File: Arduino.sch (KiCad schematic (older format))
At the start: 0 parts

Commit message: arduino module / hooking things up
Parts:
- added R? (x13): R, ~, symbol R
- added U?: ARDUINOPINS, symbol ARDUINOPINS
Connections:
- net MISO: now also R?.2
- net MOSI: now also R?.2
- net SCLK: now also R?.2
- net TACH_MEAS: now also R?.1
- new net: R?.1, U?.11 (Digital0)
- new net: R?.1, U?.12 (Digital1)
- new net: R?.1, U?.13 (Digital2)
- new net: R?.1, U?.19 (Digital8)
- new net: R?.1, U?.20 (PWM0)
- new net: R?.1, U?.21 (CS_N)
- new net: R?.1, U?.22 (MOSI)
- new net: R?.1, U?.23 (MISO)
- new net: R?.1, U?.24 (SCK)
- new net: R?.2, U?.5 (Analog0)
- new net: R?.2, U?.6 (Analog1)
- new net: R?.2, U?.7 (Analog2)
- new net: R?.2, U?.8 (Analog3)
- new net ADC_CS_N: R?.2
- new net CURR_MEAS: R?.1
- new net DAC_CS_N: R?.2
- new net FAN_EN_N: R?.2
- new net LED_EN_PWM: R?.2
- new net RELAY+: R?.2
- new net V+_ADJ_MON: R?.1
- new net V-_ADJ_MON: R?.1

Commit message: currentfan revisited
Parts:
- added R?: R, ~, symbol R
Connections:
- net at U?.11 (Digital0): now also R?.1; no longer R?.1
- net at U?.13 (Digital2): no longer R?.1
- net at U?.18 (Digital7): now also R?.1
- net at U?.21 (CS_N): now also R?.1; no longer R?.1
- net at U?.4 (9V): now also R?.2
- net FAN_MODE: now reaches R?.2
- net FAN_EN_N renamed FAN_PWM_N
- new net +12P: R?.1
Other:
- moved on the sheet: R?
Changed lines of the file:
@@
 Sheet 9 9
 Title ""
-Date "7 feb 2014"
+Date "10 feb 2014"
 Rev ""
 Comp ""
@@
 Text HLabel 6300 2950 2    60   Output ~ 0
 SCLK
-Text HLabel 6300 3400 2    60   Output ~ 0
+Text HLabel 6300 3850 2    60   Output ~ 0
 DAC_CS_N
 Text HLabel 6300 3550 2    60   Output ~ 0
 LED_EN_PWM
-Text HLabel 6300 4900 2    60   Output ~ 0
-FAN_EN_N
+Text HLabel 6300 3400 2    60   Output ~ 0
+FAN_PWM_N
 Text HLabel 2550 4600 0    60   Input ~ 0
 TACH_MEAS
@@
 L R R?
 U 1 1 52F5E804
-P 5900 4900
-F 0 "R?" V 5980 4900 40  0000 C CNN
-F 1 "R" V 5907 4901 40  0000 C CNN
-F 2 "~" V 5830 4900 30  0000 C CNN
-F 3 "~" H 5900 4900 30  0000 C CNN
-	1    5900 4900
-	0    -1   -1   0
-$EndComp
-Wire Wire Line
-	5450 4900 5650 4900
-Wire Wire Line
-	6150 4900 6300 4900
+P 5900 3400
+F 0 "R?" V 5980 3400 40  0000 C CNN
+F 1 "R" V 5907 3401 40  0000 C CNN
+F 2 "~" V 5830 3400 30  0000 C CNN
+F 3 "~" H 5900 3400 30  0000 C CNN
+	1    5900 3400
+	0    -1   -1   0
+$EndComp
+Wire Wire Line
+	5450 3400 5650 3400
+Wire Wire Line
+	6150 3400 6300 3400
 $Comp
 L R R?
@@
 L R R?
 U 1 1 52F5E82A
-P 5900 4600
-F 0 "R?" V 5980 4600 40  0000 C CNN
-F 1 "R" V 5907 4601 40  0000 C CNN
-F 2 "~" V 5830 4600 30  0000 C CNN
-F 3 "~" H 5900 4600 30  0000 C CNN
-	1    5900 4600
-	0    -1   -1   0
-$EndComp
-Wire Wire Line
-	5450 4600 5650 4600
-Wire Wire Line
-	6150 4600 6300 4600
+P 5900 4900
+F 0 "R?" V 5980 4900 40  0000 C CNN
+F 1 "R" V 5907 4901 40  0000 C CNN
+F 2 "~" V 5830 4900 30  0000 C CNN
+F 3 "~" H 5900 4900 30  0000 C CNN
+	1    5900 4900
+	0    -1   -1   0
+$EndComp
+Wire Wire Line
+	5450 4900 5650 4900
+Wire Wire Line
+	6150 4900 6300 4900
 Wire Wire Line
 	6300 4750 6150 4750
@@
 L R R?
 U 1 1 52F61E12
-P 5900 3400
-F 0 "R?" V 5980 3400 40  0000 C CNN
-F 1 "R" V 5907 3401 40  0000 C CNN
-F 2 "~" V 5830 3400 30  0000 C CNN
-F 3 "~" H 5900 3400 30  0000 C CNN
-	1    5900 3400
-	0    -1   -1   0
-$EndComp
-Wire Wire Line
-	6300 3400 6150 3400
-Wire Wire Line
-	5650 3400 5450 3400
+P 5900 3850
+F 0 "R?" V 5980 3850 40  0000 C CNN
+F 1 "R" V 5907 3851 40  0000 C CNN
+F 2 "~" V 5830 3850 30  0000 C CNN
+F 3 "~" H 5900 3850 30  0000 C CNN
+	1    5900 3850
+	0    -1   -1   0
+$EndComp
+Wire Wire Line
+	6300 3850 6150 3850
+Wire Wire Line
+	5650 3850 5450 3850
 $Comp
 L R R?
@@
 Wire Wire Line
 	5650 3700 5450 3700
+Text HLabel 6300 4900 2    60   Output ~ 0
+FAN_MODE
+$Comp
+L R R?
+U 1 1 52F919D6
+P 3000 3800
+F 0 "R?" V 3080 3800 40  0000 C CNN
+F 1 "R" V 3007 3801 40  0000 C CNN
+F 2 "~" V 2930 3800 30  0000 C CNN
+F 3 "~" H 3000 3800 30  0000 C CNN
+	1    3000 3800
+	0    -1   -1   0
+$EndComp
+Wire Wire Line
+	3400 3800 3250 3800
+Wire Wire Line
+	2750 3800 2400 3800
+Wire Wire Line
+	2400 3800 2400 3500
+$Comp
+L +12P #PWR?
+U 1 1 52F91A1B
+P 2400 3500
+F 0 "#PWR?" H 2450 3550 60  0001 C CNN
+F 1 "+12P" H 2400 3500 60  0001 C CNN
+F 2 "" H 2400 3500 60  0000 C CNN
+F 3 "" H 2400 3500 60  0001 C CNN
+F 4 "#PWR" H 2400 3470 30  0001 C CNN "Reference"
+F 5 "+12P" H 2400 3600 30  0000 C CNN "Value"
+F 6 "" H 2400 3500 60  0000 C CNN "Datasheet"
+	1    2400 3500
+	1    0    0    -1
+$EndComp
 $EndSCHEMATC

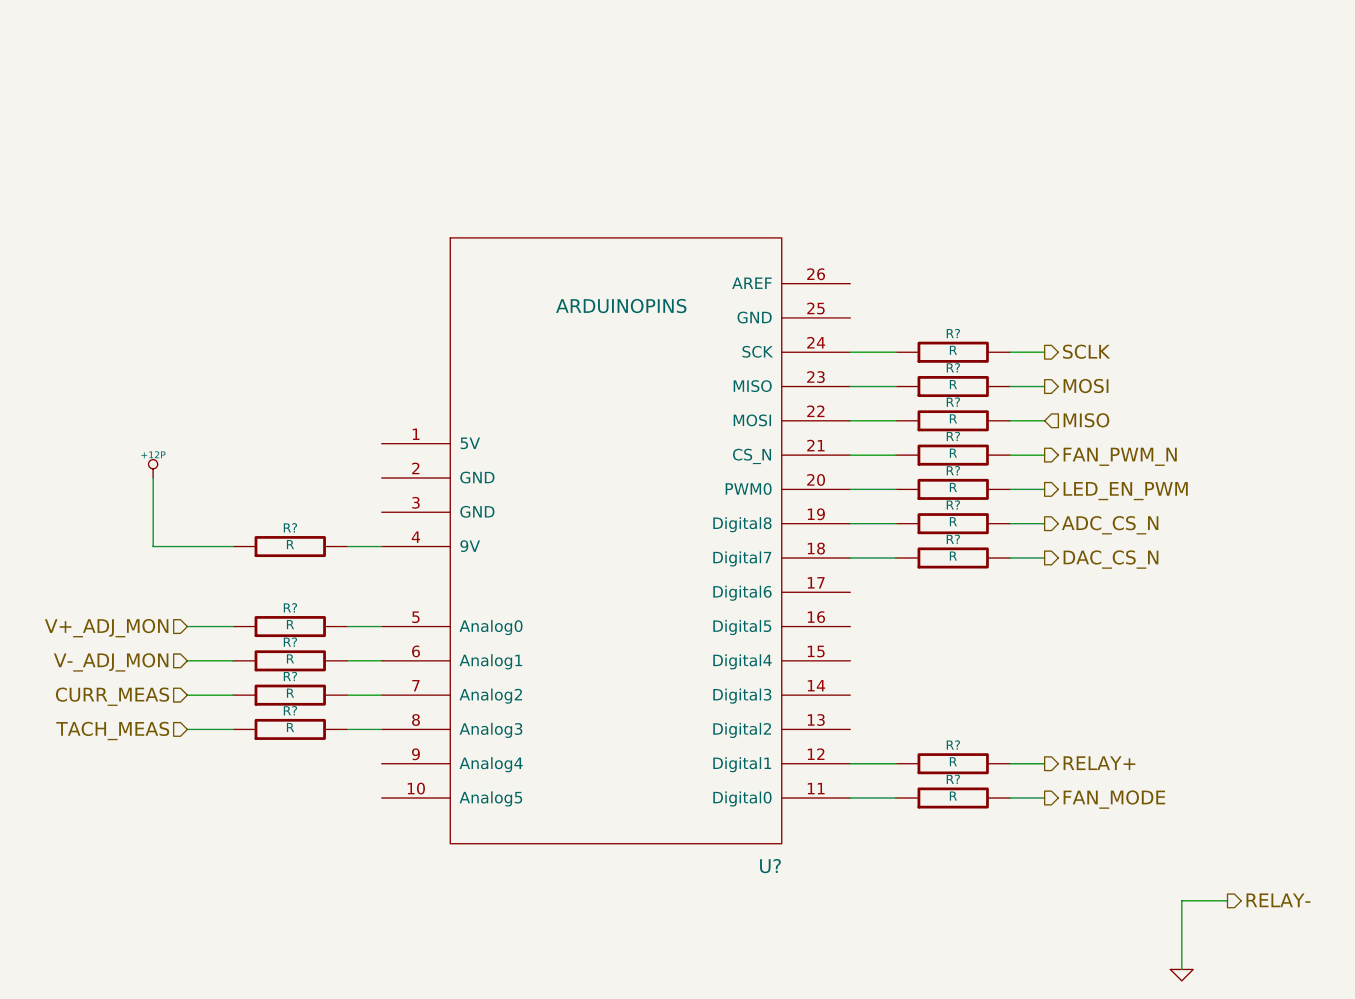
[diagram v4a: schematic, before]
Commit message: associating and placing relay module
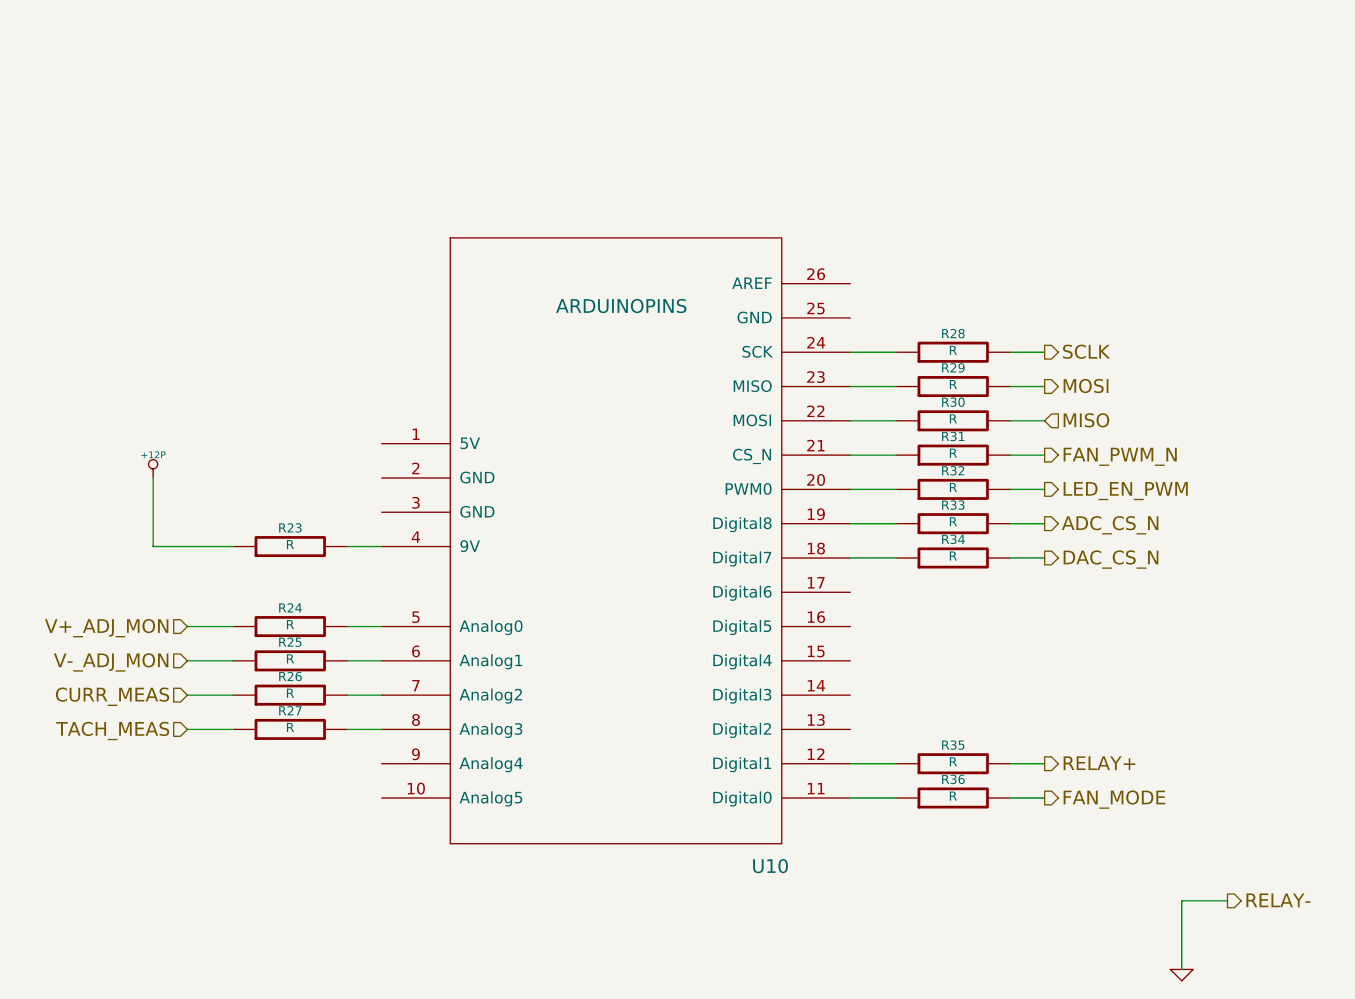
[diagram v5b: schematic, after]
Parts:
- gave numbers to parts that had none: 15
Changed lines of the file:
@@
 Sheet 9 9
 Title ""
-Date "10 feb 2014"
+Date "22 feb 2014"
 Rev ""
 Comp ""
@@
 TACH_MEAS
 $Comp
-L ARDUINOPINS U?
+L ARDUINOPINS U10
 U 1 1 52F5E6F4
 P 4450 3800
-F 0 "U?" H 5100 2400 60  0000 C CNN
+F 0 "U10" H 5100 2400 60  0000 C CNN
 F 1 "ARDUINOPINS" H 4450 4850 60  0000 C CNN
 F 2 "" H 3700 4550 60  0000 C CNN
@@
 CURR_MEAS
 $Comp
-L R R?
+L R R31
 U 1 1 52F5E804
 P 5900 3400
-F 0 "R?" V 5980 3400 40  0000 C CNN
+F 0 "R31" V 5980 3400 40  0000 C CNN
 F 1 "R" V 5907 3401 40  0000 C CNN
 F 2 "~" V 5830 3400 30  0000 C CNN
@@
 	6150 3400 6300 3400
 $Comp
-L R R?
+L R R35
 U 1 1 52F5E824
 P 5900 4750
-F 0 "R?" V 5980 4750 40  0000 C CNN
+F 0 "R35" V 5980 4750 40  0000 C CNN
 F 1 "R" V 5907 4751 40  0000 C CNN
 F 2 "~" V 5830 4750 30  0000 C CNN
@@
 $EndComp
 $Comp
-L R R?
+L R R36
 U 1 1 52F5E82A
 P 5900 4900
-F 0 "R?" V 5980 4900 40  0000 C CNN
+F 0 "R36" V 5980 4900 40  0000 C CNN
 F 1 "R" V 5907 4901 40  0000 C CNN
 F 2 "~" V 5830 4900 30  0000 C CNN
@@
 	5650 4750 5450 4750
 $Comp
-L GND #PWR?
+L GND #PWR049
 U 1 1 52F5F8B2
 P 6900 5650
-F 0 "#PWR?" H 6900 5650 30  0001 C CNN
+F 0 "#PWR049" H 6900 5650 30  0001 C CNN
 F 1 "GND" H 6900 5580 30  0001 C CNN
 F 2 "" H 6900 5650 60  0000 C CNN
@@
 	6900 5350 7100 5350
 $Comp
-L R R?
+L R R27
 U 1 1 52F5F8DC
 P 3000 4600
-F 0 "R?" V 3080 4600 40  0000 C CNN
+F 0 "R27" V 3080 4600 40  0000 C CNN
 F 1 "R" V 3007 4601 40  0000 C CNN
 F 2 "~" V 2930 4600 30  0000 C CNN
@@
 $EndComp
 $Comp
-L R R?
+L R R26
 U 1 1 52F5F8E2
 P 3000 4450
-F 0 "R?" V 3080 4450 40  0000 C CNN
+F 0 "R26" V 3080 4450 40  0000 C CNN
 F 1 "R" V 3007 4451 40  0000 C CNN
 F 2 "~" V 2930 4450 30  0000 C CNN
@@
 V-_ADJ_MON
 $Comp
-L R R?
+L R R25
 U 1 1 52F6002A
 P 3000 4300
-F 0 "R?" V 3080 4300 40  0000 C CNN
+F 0 "R25" V 3080 4300 40  0000 C CNN
 F 1 "R" V 3007 4301 40  0000 C CNN
 F 2 "~" V 2930 4300 30  0000 C CNN
@@
 $EndComp
 $Comp
-L R R?
+L R R24
 U 1 1 52F60030
 P 3000 4150
-F 0 "R?" V 3080 4150 40  0000 C CNN
+F 0 "R24" V 3080 4150 40  0000 C CNN
 F 1 "R" V 3007 4151 40  0000 C CNN
 F 2 "~" V 2930 4150 30  0000 C CNN
@@
 	2750 4300 2550 4300
 $Comp
-L R R?
+L R R30
 U 1 1 52F61DF2
 P 5900 3250
-F 0 "R?" V 5980 3250 40  0000 C CNN
+F 0 "R30" V 5980 3250 40  0000 C CNN
 F 1 "R" V 5907 3251 40  0000 C CNN
 F 2 "~" V 5830 3250 30  0000 C CNN
@@
 	6150 3250 6300 3250
 $Comp
-L R R?
+L R R29
 U 1 1 52F61DFA
 P 5900 3100
-F 0 "R?" V 5980 3100 40  0000 C CNN
+F 0 "R29" V 5980 3100 40  0000 C CNN
 F 1 "R" V 5907 3101 40  0000 C CNN
 F 2 "~" V 5830 3100 30  0000 C CNN
@@
 $EndComp
 $Comp
-L R R?
+L R R28
 U 1 1 52F61E00
 P 5900 2950
-F 0 "R?" V 5980 2950 40  0000 C CNN
+F 0 "R28" V 5980 2950 40  0000 C CNN
 F 1 "R" V 5907 2951 40  0000 C CNN
 F 2 "~" V 5830 2950 30  0000 C CNN
@@
 	5650 3100 5450 3100
 $Comp
-L R R?
+L R R34
 U 1 1 52F61E12
 P 5900 3850
-F 0 "R?" V 5980 3850 40  0000 C CNN
+F 0 "R34" V 5980 3850 40  0000 C CNN
 F 1 "R" V 5907 3851 40  0000 C CNN
 F 2 "~" V 5830 3850 30  0000 C CNN
@@
 	5650 3850 5450 3850
 $Comp
-L R R?
+L R R32
 U 1 1 52F61E4A
 P 5900 3550
-F 0 "R?" V 5980 3550 40  0000 C CNN
+F 0 "R32" V 5980 3550 40  0000 C CNN
 F 1 "R" V 5907 3551 40  0000 C CNN
 F 2 "~" V 5830 3550 30  0000 C CNN
@@
 	5650 3550 5450 3550
 $Comp
-L R R?
+L R R33
 U 1 1 52F65267
 P 5900 3700
-F 0 "R?" V 5980 3700 40  0000 C CNN
+F 0 "R33" V 5980 3700 40  0000 C CNN
 F 1 "R" V 5907 3701 40  0000 C CNN
 F 2 "~" V 5830 3700 30  0000 C CNN
@@
 FAN_MODE
 $Comp
-L R R?
+L R R23
 U 1 1 52F919D6
 P 3000 3800
-F 0 "R?" V 3080 3800 40  0000 C CNN
+F 0 "R23" V 3080 3800 40  0000 C CNN
 F 1 "R" V 3007 3801 40  0000 C CNN
 F 2 "~" V 2930 3800 30  0000 C CNN
@@
 	2400 3800 2400 3500
 $Comp
-L +12P #PWR?
+L +12P #PWR050
 U 1 1 52F91A1B
 P 2400 3500
-F 0 "#PWR?" H 2450 3550 60  0001 C CNN
+F 0 "#PWR050" H 2450 3550 60  0001 C CNN
 F 1 "+12P" H 2400 3500 60  0001 C CNN
 F 2 "" H 2400 3500 60  0000 C CNN

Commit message: associating-and-placing-the-thermocouple-module
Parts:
- added R39, R40: R, ~, symbol R
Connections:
- net at U10.15 (Digital4): now also R40.1
- net at U10.16 (Digital5): now also R39.1
- new net ~DR: R40.2
- new net ~RESET: R39.2
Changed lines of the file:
@@
 Sheet 9 9
 Title ""
-Date "22 feb 2014"
+Date "23 feb 2014"
 Rev ""
 Comp ""
@@
 	5650 4750 5450 4750
 $Comp
-L GND #PWR049
+L GND #PWR056
 U 1 1 52F5F8B2
 P 6900 5650
-F 0 "#PWR049" H 6900 5650 30  0001 C CNN
+F 0 "#PWR056" H 6900 5650 30  0001 C CNN
 F 1 "GND" H 6900 5580 30  0001 C CNN
 F 2 "" H 6900 5650 60  0000 C CNN
@@
 	2400 3800 2400 3500
 $Comp
-L +12P #PWR050
+L +12P #PWR057
 U 1 1 52F91A1B
 P 2400 3500
-F 0 "#PWR050" H 2450 3550 60  0001 C CNN
+F 0 "#PWR057" H 2450 3550 60  0001 C CNN
 F 1 "+12P" H 2400 3500 60  0001 C CNN
 F 2 "" H 2400 3500 60  0000 C CNN
@@
 	1    0    0    -1
 $EndComp
+Text HLabel 6300 4150 2    60   Output ~ 0
+~RESET
+$Comp
+L R R39
+U 1 1 530A4ED3
+P 5900 4150
+F 0 "R39" V 5980 4150 40  0000 C CNN
+F 1 "R" V 5907 4151 40  0000 C CNN
+F 2 "~" V 5830 4150 30  0000 C CNN
+F 3 "~" H 5900 4150 30  0000 C CNN
+	1    5900 4150
+	0    -1   -1   0
+$EndComp
+Wire Wire Line
+	6300 4150 6150 4150
+Wire Wire Line
+	5650 4150 5450 4150
+Text HLabel 6300 4300 2    60   Output ~ 0
+~DR
+$Comp
+L R R40
+U 1 1 530A4EDC
+P 5900 4300
+F 0 "R40" V 5980 4300 40  0000 C CNN
+F 1 "R" V 5907 4301 40  0000 C CNN
+F 2 "~" V 5830 4300 30  0000 C CNN
+F 3 "~" H 5900 4300 30  0000 C CNN
+	1    5900 4300
+	0    -1   -1   0
+$EndComp
+Wire Wire Line
+	6300 4300 6150 4300
+Wire Wire Line
+	5650 4300 5450 4300
 $EndSCHEMATC
